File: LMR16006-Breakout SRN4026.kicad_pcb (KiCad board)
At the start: 2 copper layers, 21 x 21 mm, 17 parts, among them P1 CONN_01X04, U1 LMR16006

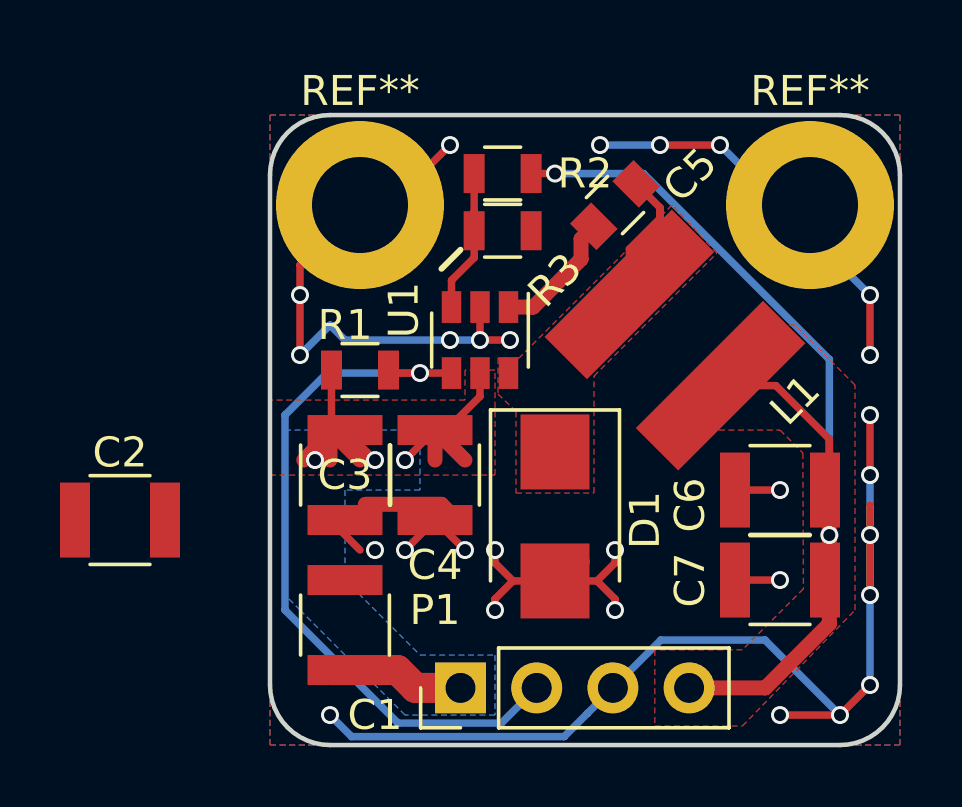
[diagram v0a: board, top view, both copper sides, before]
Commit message: change input and output capacitors from 1206 to 1210 footprints, change inductor from srn4026 to srn6045 footprint (to get Isat > 1.6A at 22µH)
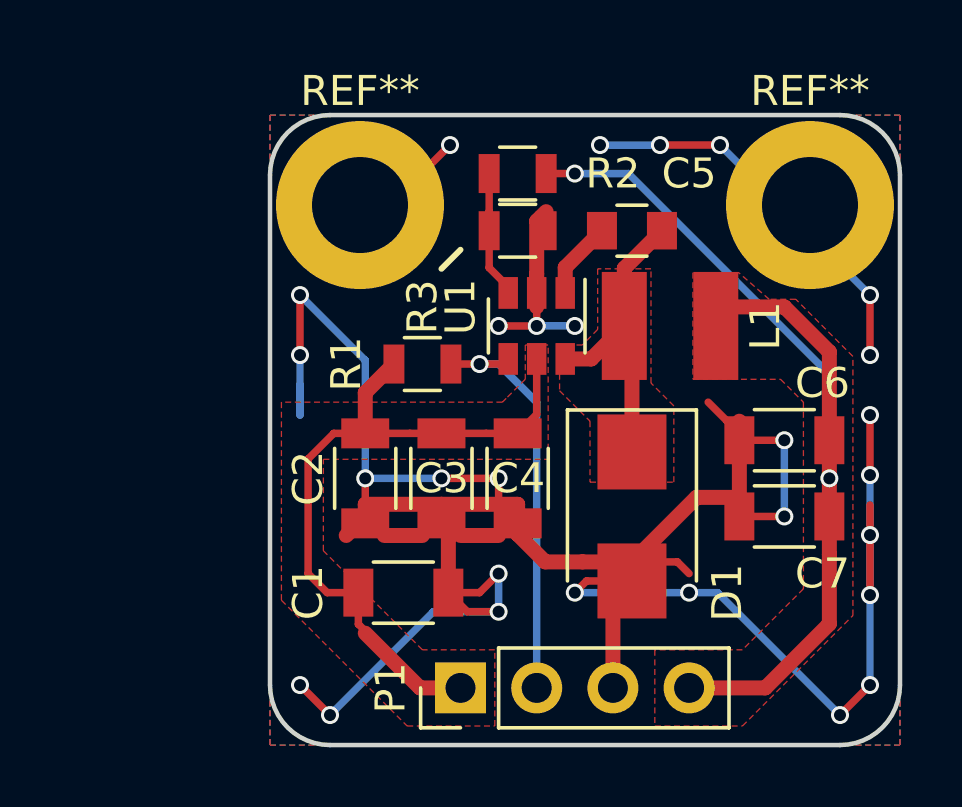
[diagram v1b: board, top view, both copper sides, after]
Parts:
- C1, C2, C3, C4, C6, C7: footprint Capacitors_SMD:C_1210 -> Capacitors_SMD:C_1206
- L1: footprint inductors:SRN6045 -> inductors:SRN4026
- moved C2 8.29 mm to (123.2, 101.1), turned to 270 degrees
- moved C3 3.22 mm to (125.7, 101.1)
- moved C4 2.76 mm to (128.3, 101.1)
- moved D1 2.56 mm to (132.1, 102.4)
- moved C1 2.22 mm to (124.4, 104.9), turned to 0 degrees
- moved C7 2.12 mm to (137.1, 102.4)
- moved R1 2.09 mm to (125.1, 97.3)
- moved U1 1.95 mm to (128.9, 96.0)
- moved C6 1.67 mm to (137.1, 99.8)
- moved C5 1.02 mm to (132.1, 92.9), turned to 0 degrees
- moved R2 0.50 mm to (128.3, 91.0)
- moved R3 0.50 mm to (128.3, 92.9)
- moved L1 0.50 mm to (133.3, 96.0), turned to 180 degrees
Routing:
- net GND: track 86.3 -> 121.3 mm
- net /SHDN: track 24.2 -> 13.9 mm
- net VCC: track 19.8 -> 24.7 mm, vias 3 -> 0
- net Net-(C5-Pad1): track 4.35 -> 2.58 mm
- net VAA: track 35.7 -> 34.7 mm
- net Net-(R2-Pad2): track 5.06 -> 4.54 mm
- removed copper zone on B.Cu, net VCC
